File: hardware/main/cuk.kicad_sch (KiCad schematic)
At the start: 30 parts, among them Q401 BSC093N15NS5, Q402 BSC093N15NS5

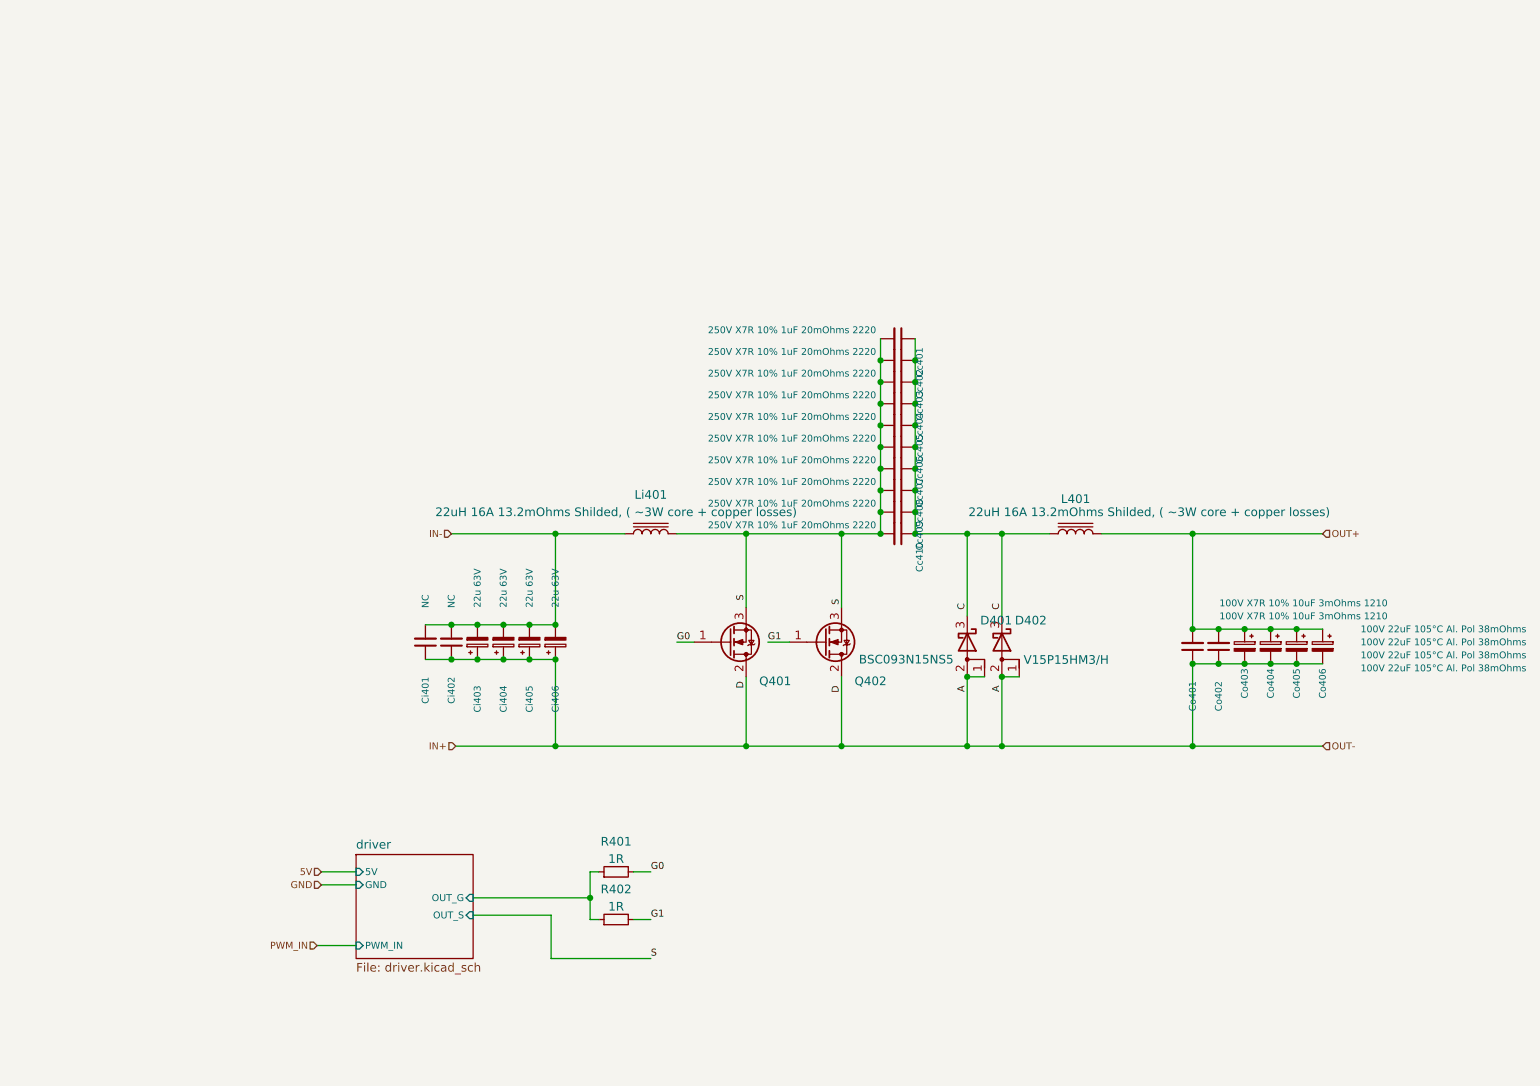
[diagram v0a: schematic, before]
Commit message: Schematics: finalize Analog Snubber and Supplies
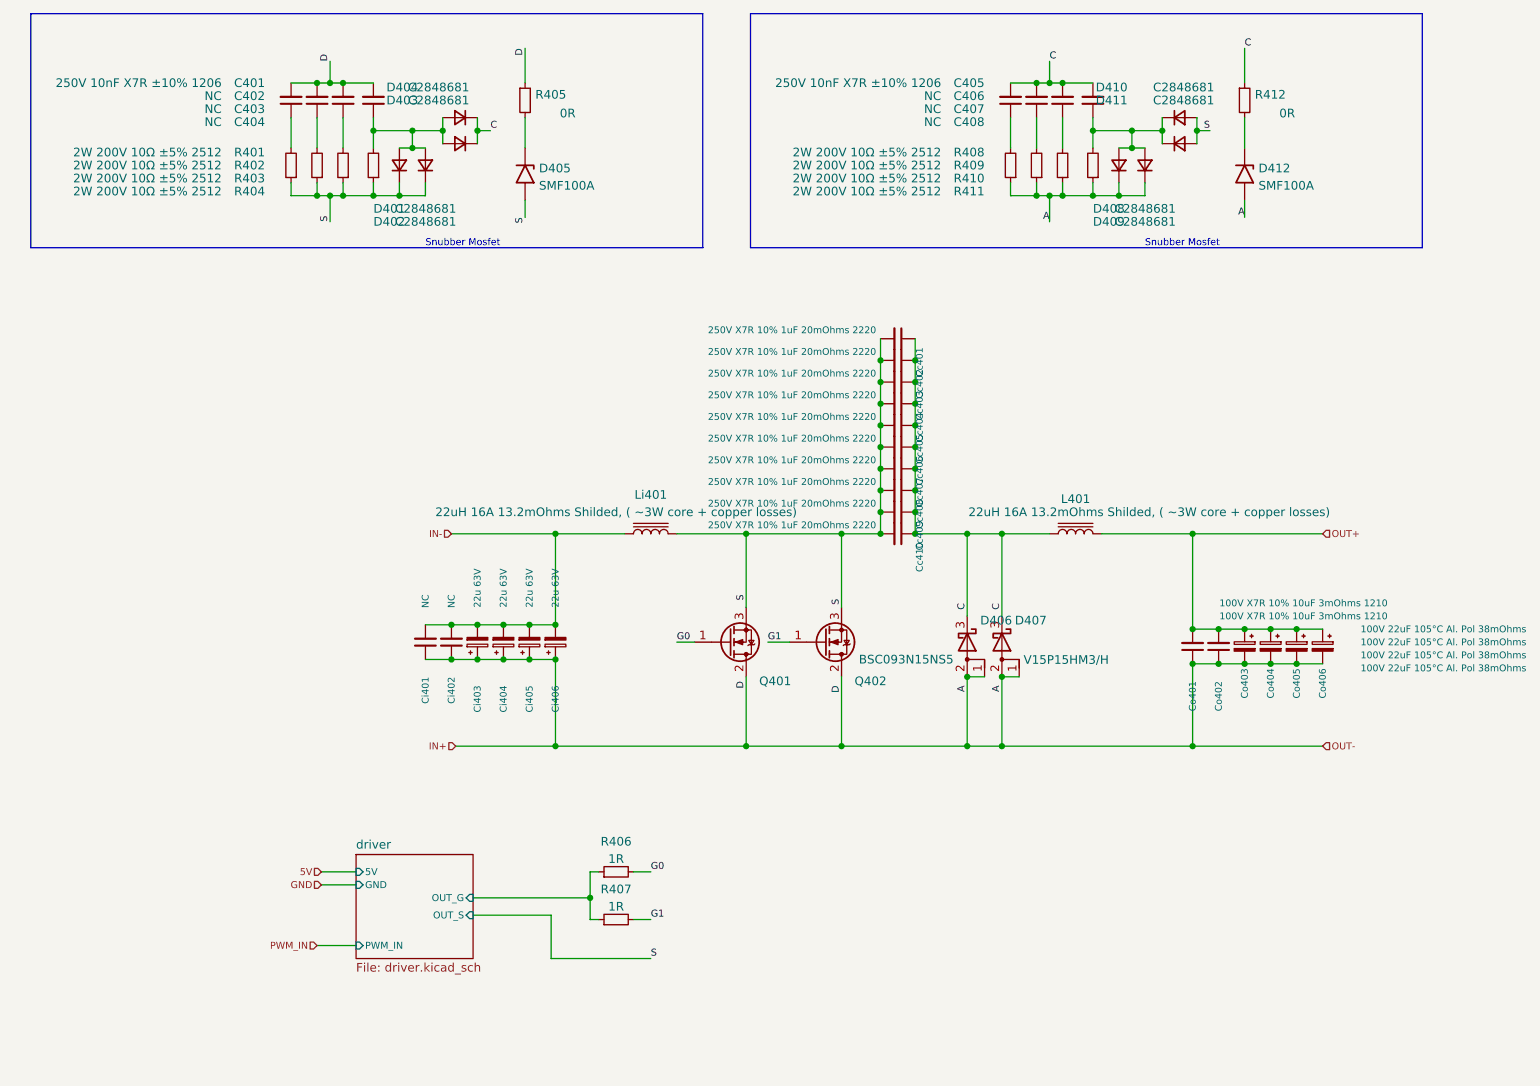
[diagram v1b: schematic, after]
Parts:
- added C401, C405: 250V 10nF X7R ±10% 1206, symbol Device:C_Small
- added C402, C403, C404, C406, C407, C408: NC, symbol Device:C_Small
- added D401, D402, D403, D404, D408, D409, D410, D411: C2848681, symbol Device:D_Small
- added D405, D412: SMF100A, Diode_SMD:D_SOD-123F, symbol Diode:SMF18A
- added R401, R402, R403, R404, R408, R409, R410, R411: 2W 200V 10Ω ±5% 2512, symbol Device:R_Small
- added R405, R412: 0R, symbol Device:R_Small
- renumbered D401 to D406, D402 to D407, R401 to R406, R402 to R407
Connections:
- net C: now also C405.2, C406.2, C407.2, C408.2, D403.1 (K), D404.1 (K), R412.1
- net IN+: now also C401.2, C402.2, C403.2, C404.2, D408.1 (K), D409.1 (K), D412.2 (A2), R405.1, R408.1, R409.1, R410.1, R411.1
- net S: now also D401.1 (K), D402.1 (K), D405.2 (A2), D410.2 (A), D411.2 (A), R401.1, R402.1, R403.1, R404.1
- new net: D412.1 (A1), R412.2
- new net: C402.1, R402.2
- new net: C404.1, D401.2 (A), D402.2 (A), D403.2 (A), D404.2 (A), R404.2
- new net: C407.1, R410.2
- new net: C405.1, R408.2
- new net: C401.1, R401.2
- new net: C408.1, D408.2 (A), D409.2 (A), D410.1 (K), D411.1 (K), R411.2
- new net: C406.1, R409.2
- new net: C403.1, R403.2
- new net: D405.1 (A1), R405.2
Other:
- note added: "Snubber Mosfet"

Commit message: Schematics: Modified component values
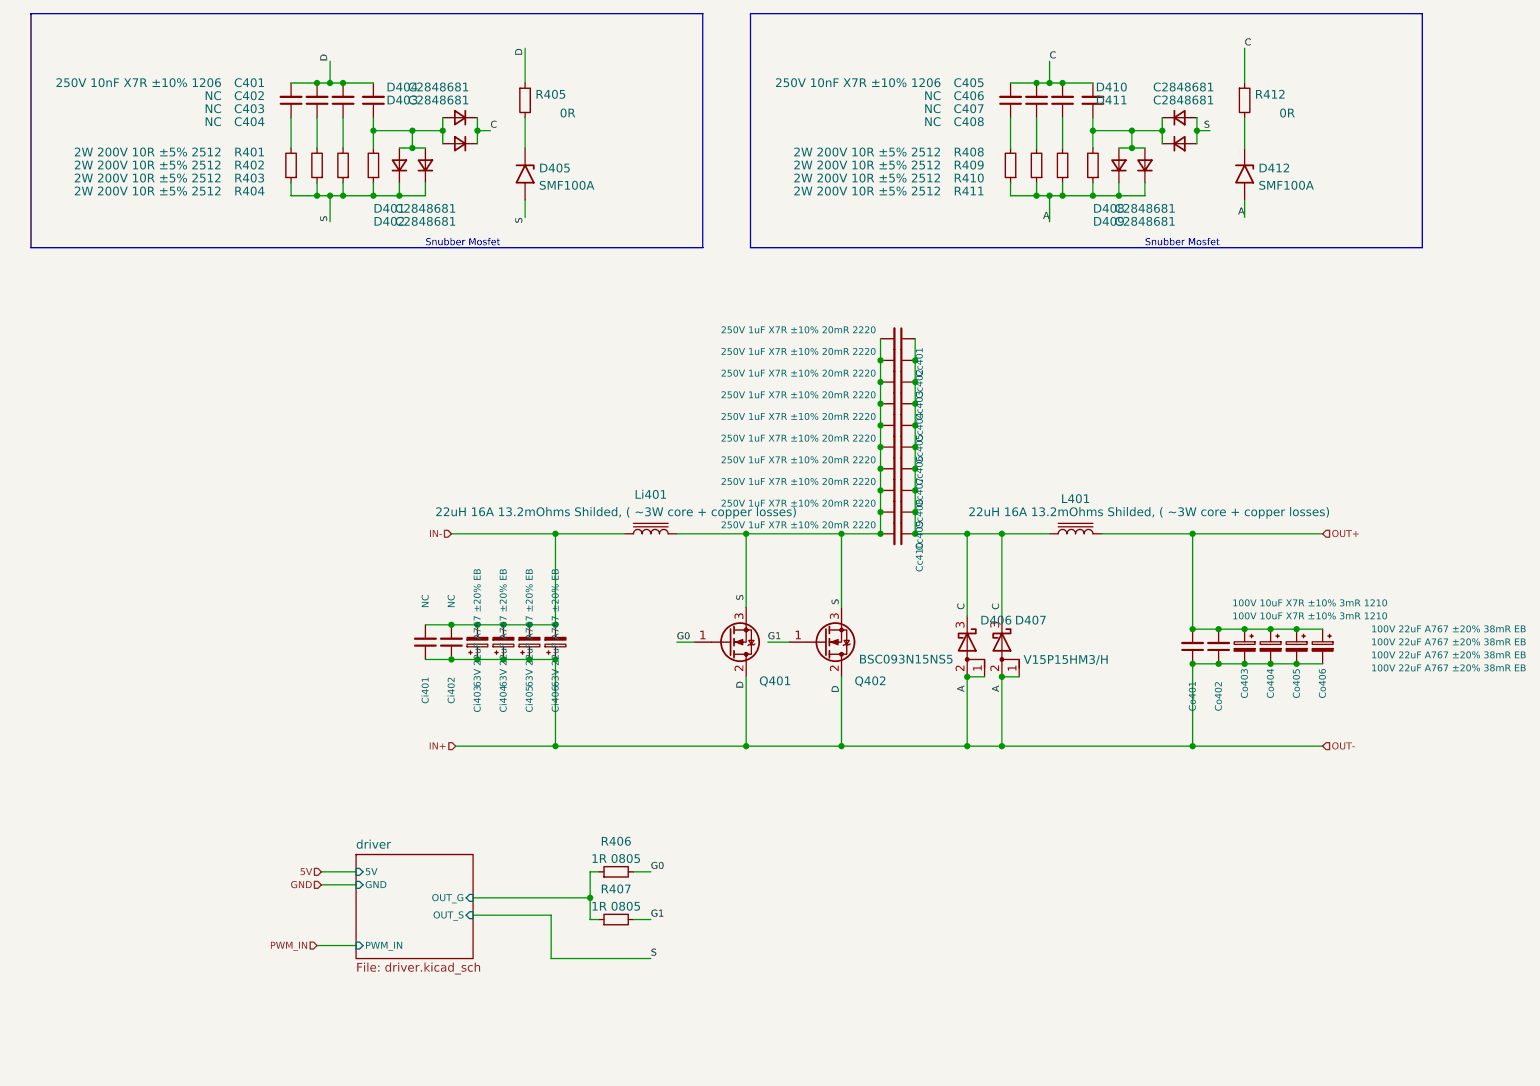
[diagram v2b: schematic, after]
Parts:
- Cc401, Cc402, Cc403, Cc404, Cc405, Cc406, Cc407, Cc408, Cc409, Cc410: value 250V X7R 10% 1uF 20mOhms 2220 -> 250V 1uF X7R ±10% 20mR 2220
- Ci403, Ci404, Ci405, Ci406: value 22u 63V -> 63V 22uF A767 ±20% EB
- Co401, Co402: value 100V X7R 10% 10uF 3mOhms 1210 -> 100V 10uF X7R ±10% 3mR 1210
- Co403, Co404, Co405, Co406: value 100V 22uF 105°C Al. Pol 38mOhms -> 100V 22uF A767 ±20% 38mR EB
- R401, R402, R403, R404, R408, R409, R410, R411: value 2W 200V 10Ω ±5% 2512 -> 2W 200V 10R ±5% 2512
- R406, R407: value 1R -> 1R 0805
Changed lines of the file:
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@@
       (effects (font (size 1 1)) (justify left))
     )
-    (property "Value" "100V X7R 10% 10uF 3mOhms 1210" (id 1) (at 220.98 112.395 0)
+    (property "Value" "100V 10uF X7R ±10% 3mR 1210" (id 1) (at 220.98 112.395 0)
       (effects (font (size 1 1)) (justify left))
     )
@@
       (effects (font (size 1.27 1.27)) (justify left))
     )
-    (property "Value" "2W 200V 10Ω ±5% 2512" (id 1) (at 50.165 46.355 0)
+    (property "Value" "2W 200V 10R ±5% 2512" (id 1) (at 50.165 46.355 0)
       (effects (font (size 1.27 1.27)) (justify left))
     )
@@
       (effects (font (size 1 1)) (justify left))
     )
-    (property "Value" "22u 63V" (id 1) (at 87.63 105.41 90)
+    (property "Value" "63V 22uF A767 ±20% EB" (id 1) (at 87.63 105.41 90)
       (effects (font (size 1 1)) (justify left))
     )
@@
       (effects (font (size 1 1)) (justify left))
     )
-    (property "Value" "250V X7R 10% 1uF 20mOhms 2220" (id 1) (at 146.05 73.66 90)
+    (property "Value" "250V 1uF X7R ±10% 20mR 2220" (id 1) (at 146.05 73.66 90)
       (effects (font (size 1 1)) (justify right))
     )
@@
       (effects (font (size 1 1)) (justify left))
     )
-    (property "Value" "22u 63V" (id 1) (at 99.06 105.41 90)
+    (property "Value" "63V 22uF A767 ±20% EB" (id 1) (at 99.06 105.41 90)
       (effects (font (size 1 1)) (justify left))
     )
@@
       (effects (font (size 1.27 1.27)) (justify left))
     )
-    (property "Value" "2W 200V 10Ω ±5% 2512" (id 1) (at 155.575 44.45 0)
+    (property "Value" "2W 200V 10R ±5% 2512" (id 1) (at 155.575 44.45 0)
       (effects (font (size 1.27 1.27)) (justify left))
     )
@@
       (effects (font (size 1 1)) (justify left))
     )
-    (property "Value" "250V X7R 10% 1uF 20mOhms 2220" (id 1) (at 146.05 70.485 90)
+    (property "Value" "250V 1uF X7R ±10% 20mR 2220" (id 1) (at 146.05 70.485 90)
       (effects (font (size 1 1)) (justify right))
     )
@@
     (in_bom yes) (on_board yes) (fields_autoplaced)
     (property "Reference" "R406" (id 0) (at 107.95 145.4236 90))
-    (property "Value" "1R" (id 1) (at 107.95 147.9605 90))
+    (property "Value" "1R 0805" (id 1) (at 107.95 147.9605 90))
     (property "Footprint" "" (id 2) (at 107.95 149.86 0)
       (effects (font (size 1.27 1.27)) hide)
@@
       (effects (font (size 1 1)) (justify left))
     )
-    (property "Value" "250V X7R 10% 1uF 20mOhms 2220" (id 1) (at 146.05 80.01 90)
+    (property "Value" "250V 1uF X7R ±10% 20mR 2220" (id 1) (at 146.05 80.01 90)
       (effects (font (size 1 1)) (justify right))
     )
@@
       (effects (font (size 1 1)) (justify left))
     )
-    (property "Value" "22u 63V" (id 1) (at 91.44 105.41 90)
+    (property "Value" "63V 22uF A767 ±20% EB" (id 1) (at 91.44 105.41 90)
       (effects (font (size 1 1)) (justify left))
     )
@@
       (effects (font (size 1.27 1.27)) (justify left))
     )
-    (property "Value" "2W 200V 10Ω ±5% 2512" (id 1) (at 50.165 44.45 0)
+    (property "Value" "2W 200V 10R ±5% 2512" (id 1) (at 50.165 44.45 0)
       (effects (font (size 1.27 1.27)) (justify left))
     )
@@
       (effects (font (size 1.27 1.27)) (justify left))
     )
-    (property "Value" "2W 200V 10Ω ±5% 2512" (id 1) (at 50.165 50.165 0)
+    (property "Value" "2W 200V 10R ±5% 2512" (id 1) (at 50.165 50.165 0)
       (effects (font (size 1.27 1.27)) (justify left))
     )
@@
       (effects (font (size 1 1)) (justify left))
     )
-    (property "Value" "100V X7R 10% 10uF 3mOhms 1210" (id 1) (at 220.98 110.49 0)
+    (property "Value" "100V 10uF X7R ±10% 3mR 1210" (id 1) (at 220.98 110.49 0)
       (effects (font (size 1 1)) (justify left))
     )
@@
     (in_bom yes) (on_board yes) (fields_autoplaced)
     (property "Reference" "R407" (id 0) (at 107.95 152.4086 90))
-    (property "Value" "1R" (id 1) (at 107.95 154.9455 90))
+    (property "Value" "1R 0805" (id 1) (at 107.95 154.9455 90))
     (property "Footprint" "" (id 2) (at 107.95 156.845 0)
       (effects (font (size 1.27 1.27)) hide)
@@
       (effects (font (size 1 1)) (justify left))
     )
-    (property "Value" "100V 22uF 105°C Al. Pol 38mOhms" (id 1) (at 241.3 116.205 0)
+    (property "Value" "100V 22uF A767  ±20% 38mR EB" (id 1) (at 241.3 116.205 0)
       (effects (font (size 1 1)) (justify left))
     )
@@
       (effects (font (size 1 1)) (justify left))
     )
-    (property "Value" "22u 63V" (id 1) (at 95.25 105.41 90)
+    (property "Value" "63V 22uF A767 ±20% EB" (id 1) (at 95.25 105.41 90)
       (effects (font (size 1 1)) (justify left))
     )
@@
       (effects (font (size 1 1)) (justify left))
     )
-    (property "Value" "250V X7R 10% 1uF 20mOhms 2220" (id 1) (at 146.05 83.185 90)
+    (property "Value" "250V 1uF X7R ±10% 20mR 2220" (id 1) (at 146.05 83.185 90)
       (effects (font (size 1 1)) (justify right))
     )
@@
       (effects (font (size 1 1)) (justify left))
     )
-    (property "Value" "100V 22uF 105°C Al. Pol 38mOhms" (id 1) (at 241.3 120.015 0)
+    (property "Value" "100V 22uF A767  ±20% 38mR EB" (id 1) (at 241.3 120.015 0)
       (effects (font (size 1 1)) (justify left))
     )
@@
       (effects (font (size 1.27 1.27)) (justify left))
     )
-    (property "Value" "2W 200V 10Ω ±5% 2512" (id 1) (at 50.165 48.26 0)
+    (property "Value" "2W 200V 10R ±5% 2512" (id 1) (at 50.165 48.26 0)
       (effects (font (size 1.27 1.27)) (justify left))
     )
@@
       (effects (font (size 1 1)) (justify left))
     )
-    (property "Value" "250V X7R 10% 1uF 20mOhms 2220" (id 1) (at 146.05 89.535 90)
+    (property "Value" "250V 1uF X7R ±10% 20mR 2220" (id 1) (at 146.05 89.535 90)
       (effects (font (size 1 1)) (justify right))
     )
@@
       (effects (font (size 1.27 1.27)) (justify left))
     )
-    (property "Value" "2W 200V 10Ω ±5% 2512" (id 1) (at 155.575 46.355 0)
+    (property "Value" "2W 200V 10R ±5% 2512" (id 1) (at 155.575 46.355 0)
       (effects (font (size 1.27 1.27)) (justify left))
     )
@@
       (effects (font (size 1.27 1.27)) (justify left))
     )
-    (property "Value" "2W 200V 10Ω ±5% 2512" (id 1) (at 155.575 50.165 0)
+    (property "Value" "2W 200V 10R ±5% 2512" (id 1) (at 155.575 50.165 0)
       (effects (font (size 1.27 1.27)) (justify left))
     )
@@
       (effects (font (size 1 1)) (justify left))
     )
-    (property "Value" "250V X7R 10% 1uF 20mOhms 2220" (id 1) (at 146.05 99.06 90)
+    (property "Value" "250V 1uF X7R ±10% 20mR 2220" (id 1) (at 146.05 99.06 90)
       (effects (font (size 1 1)) (justify right))
     )
@@
       (effects (font (size 1 1)) (justify left))
     )
-    (property "Value" "100V 22uF 105°C Al. Pol 38mOhms" (id 1) (at 241.3 114.3 0)
+    (property "Value" "100V 22uF A767  ±20% 38mR EB" (id 1) (at 241.3 114.3 0)
       (effects (font (size 1 1)) (justify left))
     )
@@
       (effects (font (size 1 1)) (justify left))
     )
-    (property "Value" "250V X7R 10% 1uF 20mOhms 2220" (id 1) (at 146.05 76.835 90)
+    (property "Value" "250V 1uF X7R ±10% 20mR 2220" (id 1) (at 146.05 76.835 90)
       (effects (font (size 1 1)) (justify right))
     )
@@
       (effects (font (size 1 1)) (justify left))
     )
-    (property "Value" "100V 22uF 105°C Al. Pol 38mOhms" (id 1) (at 241.3 118.11 0)
+    (property "Value" "100V 22uF A767  ±20% 38mR EB" (id 1) (at 241.3 118.11 0)
       (effects (font (size 1 1)) (justify left))
     )
@@
       (effects (font (size 1.27 1.27)) (justify left))
     )
-    (property "Value" "2W 200V 10Ω ±5% 2512" (id 1) (at 155.575 48.26 0)
+    (property "Value" "2W 200V 10R ±5% 2512" (id 1) (at 155.575 48.26 0)
       (effects (font (size 1.27 1.27)) (justify left))
     )
@@
       (effects (font (size 1 1)) (justify left))
     )
-    (property "Value" "250V X7R 10% 1uF 20mOhms 2220" (id 1) (at 146.05 86.36 90)
+    (property "Value" "250V 1uF X7R ±10% 20mR 2220" (id 1) (at 146.05 86.36 90)
       (effects (font (size 1 1)) (justify right))
     )
@@
       (effects (font (size 1 1)) (justify left))
     )
-    (property "Value" "250V X7R 10% 1uF 20mOhms 2220" (id 1) (at 146.05 92.71 90)
+    (property "Value" "250V 1uF X7R ±10% 20mR 2220" (id 1) (at 146.05 92.71 90)
       (effects (font (size 1 1)) (justify right))
     )
@@
       (effects (font (size 1 1)) (justify left))
     )
-    (property "Value" "250V X7R 10% 1uF 20mOhms 2220" (id 1) (at 146.05 95.885 90)
+    (property "Value" "250V 1uF X7R ±10% 20mR 2220" (id 1) (at 146.05 95.885 90)
       (effects (font (size 1 1)) (justify right))
     )
